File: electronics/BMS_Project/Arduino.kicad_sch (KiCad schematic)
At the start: 1 part

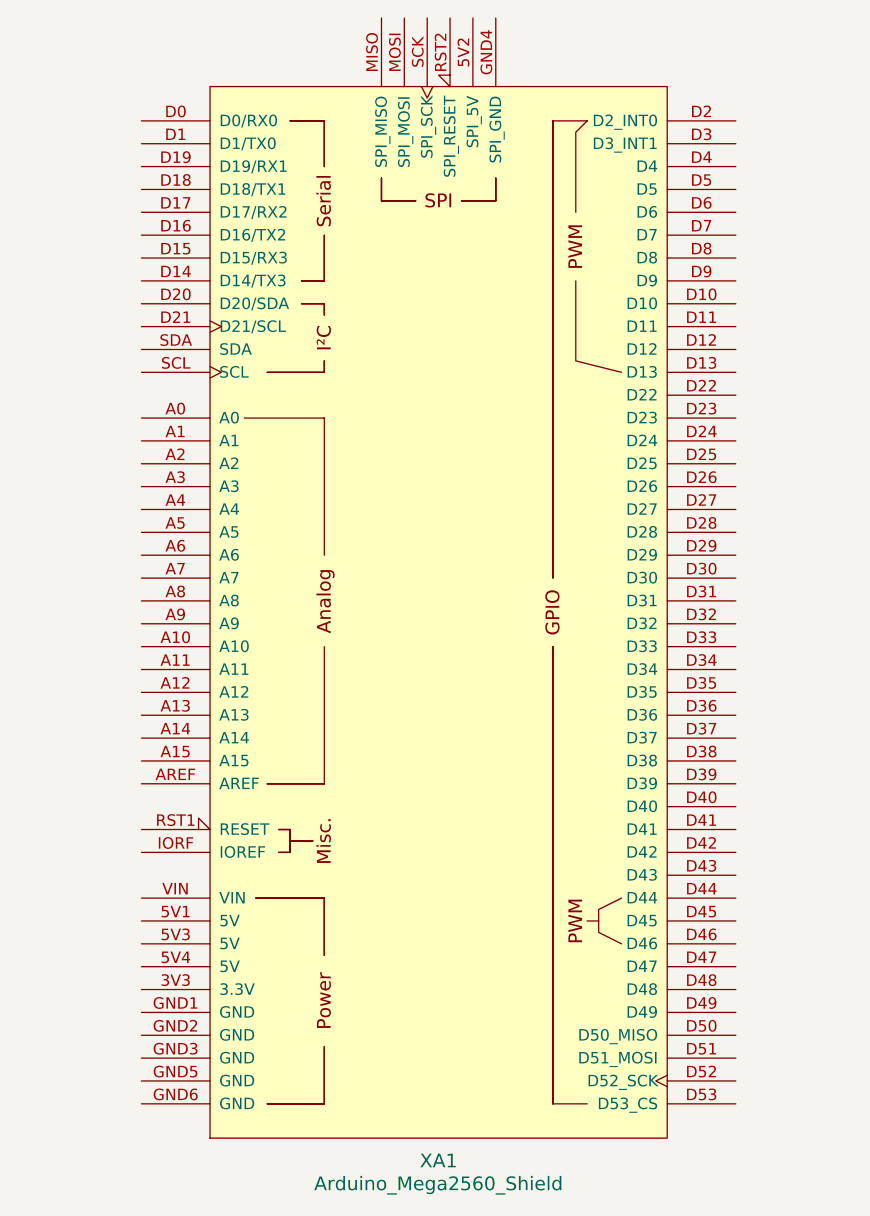
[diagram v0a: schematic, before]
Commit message: Started working on schematic segmentation and added first labels
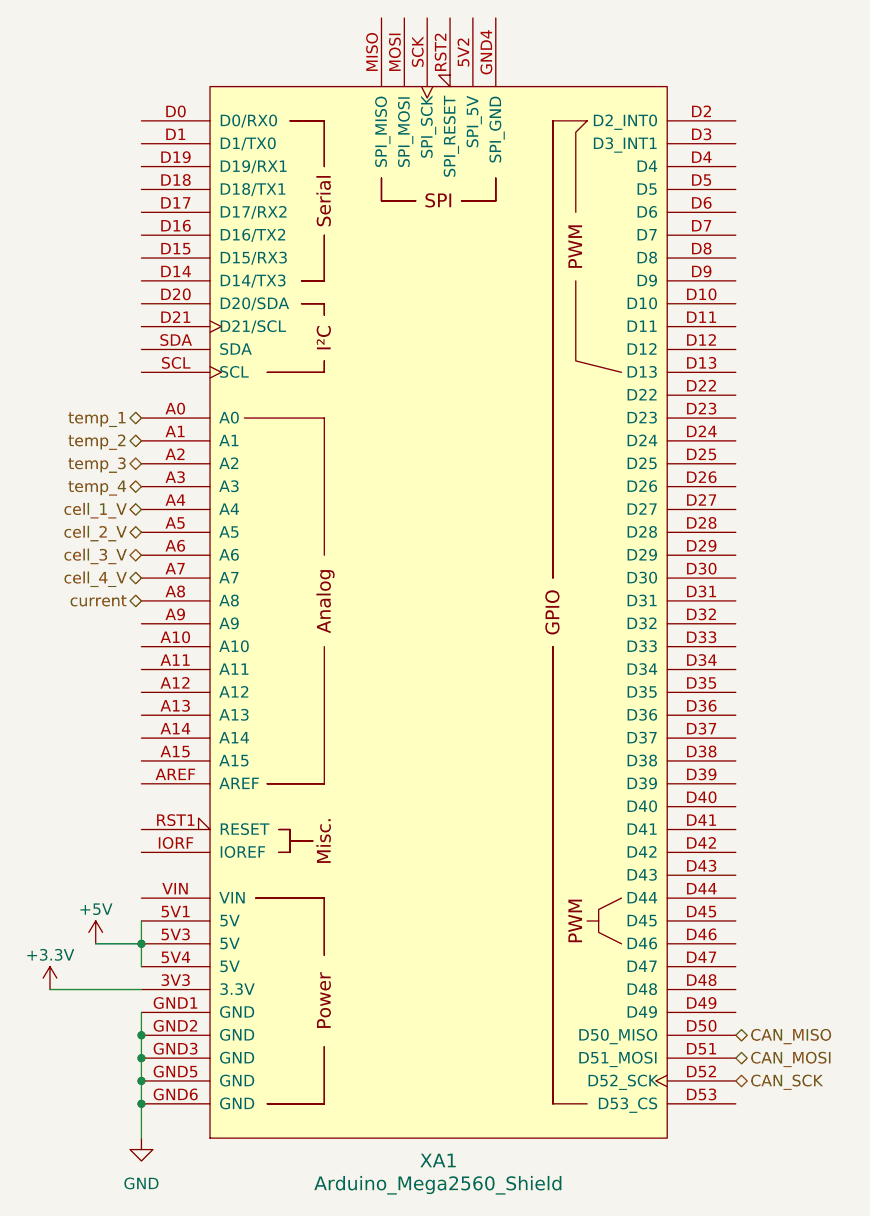
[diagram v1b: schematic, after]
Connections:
- net +3.3V: now reaches XA1.3V3 (3.3V)
- net +5V: now reaches XA1.5V1 (5V)
- net +5V: now also XA1.5V3 (5V), XA1.5V4 (5V)
- net temp_1: now reaches XA1.A0
- net temp_2: now reaches XA1.A1
- net temp_3: now reaches XA1.A2
- net temp_4: now reaches XA1.A3
- net cell_1_V: now reaches XA1.A4
- net cell_2_V: now reaches XA1.A5
- net cell_3_V: now reaches XA1.A6
- net cell_4_V: now reaches XA1.A7
- net current: now reaches XA1.A8
- net CAN_MISO: now reaches XA1.D50 (D50_MISO)
- net CAN_MOSI: now reaches XA1.D51 (D51_MOSI)
- net CAN_SCK: now reaches XA1.D52 (D52_SCK)
- net GND: now reaches XA1.GND1 (GND)
- net GND: now also XA1.GND2 (GND), XA1.GND3 (GND), XA1.GND5 (GND), XA1.GND6 (GND)
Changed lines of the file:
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@@
     (comment 2 "Edited: ")
+  )
+  (junction (at 82.55 132.08) (diameter 0) (color 0 0 0 0)
+  )
+  (junction (at 82.55 149.86) (diameter 0) (color 0 0 0 0)
+  )
+  (junction (at 82.55 142.24) (diameter 0) (color 0 0 0 0)
+  )
+  (junction (at 82.55 147.32) (diameter 0) (color 0 0 0 0)
+  )
+  (junction (at 82.55 144.78) (diameter 0) (color 0 0 0 0)
+  )
+  (wire (pts (xy 82.55 139.7) (xy 82.55 142.24))
+    (stroke (width 0) (type default))
+  )
+  (wire (pts (xy 82.55 147.32) (xy 82.55 149.86))
+    (stroke (width 0) (type default))
+  )
+  (wire (pts (xy 72.39 137.16) (xy 82.55 137.16))
+    (stroke (width 0) (type default))
+  )
+  (wire (pts (xy 77.47 132.08) (xy 82.55 132.08))
+    (stroke (width 0) (type default))
+  )
+  (wire (pts (xy 82.55 142.24) (xy 82.55 144.78))
+    (stroke (width 0) (type default))
+  )
+  (wire (pts (xy 82.55 149.86) (xy 82.55 153.67))
+    (stroke (width 0) (type default))
+  )
+  (wire (pts (xy 82.55 132.08) (xy 82.55 134.62))
+    (stroke (width 0) (type default))
+  )
+  (wire (pts (xy 82.55 129.54) (xy 82.55 132.08))
+    (stroke (width 0) (type default))
+  )
+  (wire (pts (xy 82.55 144.78) (xy 82.55 147.32))
+    (stroke (width 0) (type default))
+  )
+  (hierarchical_label "temp_1" (shape bidirectional) (at 82.55 73.66 180) (fields_autoplaced)
+    (effects (font (size 1.27 1.27)) (justify right))
+  )
+  (hierarchical_label "CAN_MOSI" (shape bidirectional) (at 148.59 144.78 0) (fields_autoplaced)
+    (effects (font (size 1.27 1.27)) (justify left))
+  )
+  (hierarchical_label "current" (shape bidirectional) (at 82.55 93.98 180) (fields_autoplaced)
+    (effects (font (size 1.27 1.27)) (justify right))
+  )
+  (hierarchical_label "cell_1_V" (shape bidirectional) (at 82.55 83.82 180) (fields_autoplaced)
+    (effects (font (size 1.27 1.27)) (justify right))
+  )
+  (hierarchical_label "temp_3" (shape bidirectional) (at 82.55 78.74 180) (fields_autoplaced)
+    (effects (font (size 1.27 1.27)) (justify right))
+  )
+  (hierarchical_label "cell_3_V" (shape bidirectional) (at 82.55 88.9 180) (fields_autoplaced)
+    (effects (font (size 1.27 1.27)) (justify right))
+  )
+  (hierarchical_label "temp_4" (shape bidirectional) (at 82.55 81.28 180) (fields_autoplaced)
+    (effects (font (size 1.27 1.27)) (justify right))
+  )
+  (hierarchical_label "cell_2_V" (shape bidirectional) (at 82.55 86.36 180) (fields_autoplaced)
+    (effects (font (size 1.27 1.27)) (justify right))
+  )
+  (hierarchical_label "cell_4_V" (shape bidirectional) (at 82.55 91.44 180) (fields_autoplaced)
+    (effects (font (size 1.27 1.27)) (justify right))
+  )
+  (hierarchical_label "CAN_MISO" (shape bidirectional) (at 148.59 142.24 0) (fields_autoplaced)
+    (effects (font (size 1.27 1.27)) (justify left))
+  )
+  (hierarchical_label "temp_2" (shape bidirectional) (at 82.55 76.2 180) (fields_autoplaced)
+    (effects (font (size 1.27 1.27)) (justify right))
+  )
+  (hierarchical_label "CAN_SCK" (shape bidirectional) (at 148.59 147.32 0) (fields_autoplaced)
+    (effects (font (size 1.27 1.27)) (justify left))
+  )
+  (symbol (lib_id "power:+3.3V") (at 72.39 137.16 0) (unit 1)
+    (in_bom yes) (on_board yes) (dnp no) (fields_autoplaced)
+    (property "Reference" "#PWR023" (at 72.39 140.97 0)
+      (effects (font (size 1.27 1.27)) hide)
+    )
+    (property "Value" "+3.3V" (at 72.39 133.35 0)
+      (effects (font (size 1.27 1.27)))
+    )
+    (property "Footprint" "" (at 72.39 137.16 0)
+      (effects (font (size 1.27 1.27)) hide)
+    )
+    (property "Datasheet" "" (at 72.39 137.16 0)
+      (effects (font (size 1.27 1.27)) hide)
+    )
+    (pin "1")
+    (instances
+      (project "BMS_Project"
+        (path "/524e7f14-feb0-4ca2-9425-a347c869bfa6/991268b7-e362-463f-9f04-bcec0fe70615"
+          (reference "#PWR023") (unit 1)
+        )
+      )
+    )
+  )
+  (symbol (lib_id "power:GND") (at 82.55 153.67 0) (unit 1)
+    (in_bom yes) (on_board yes) (dnp no) (fields_autoplaced)
+    (property "Reference" "#PWR022" (at 82.55 160.02 0)
+      (effects (font (size 1.27 1.27)) hide)
+    )
+    (property "Value" "GND" (at 82.55 158.75 0)
+      (effects (font (size 1.27 1.27)))
+    )
+    (property "Footprint" "" (at 82.55 153.67 0)
+      (effects (font (size 1.27 1.27)) hide)
+    )
+    (property "Datasheet" "" (at 82.55 153.67 0)
+      (effects (font (size 1.27 1.27)) hide)
+    )
+    (pin "1")
+    (instances
+      (project "BMS_Project"
+        (path "/524e7f14-feb0-4ca2-9425-a347c869bfa6/991268b7-e362-463f-9f04-bcec0fe70615"
+          (reference "#PWR022") (unit 1)
+        )
+      )
+    )
+  )
+  (symbol (lib_id "power:+5V") (at 77.47 132.08 0) (unit 1)
+    (in_bom yes) (on_board yes) (dnp no) (fields_autoplaced)
+    (property "Reference" "#PWR024" (at 77.47 135.89 0)
+      (effects (font (size 1.27 1.27)) hide)
+    )
+    (property "Value" "+5V" (at 77.47 128.27 0)
+      (effects (font (size 1.27 1.27)))
+    )
+    (property "Footprint" "" (at 77.47 132.08 0)
+      (effects (font (size 1.27 1.27)) hide)
+    )
+    (property "Datasheet" "" (at 77.47 132.08 0)
+      (effects (font (size 1.27 1.27)) hide)
+    )
+    (pin "1")
+    (instances
+      (project "BMS_Project"
+        (path "/524e7f14-feb0-4ca2-9425-a347c869bfa6/991268b7-e362-463f-9f04-bcec0fe70615"
+          (reference "#PWR024") (unit 1)
+        )
+      )
+    )
   )
   (symbol (lib_id "arduino-library:Arduino_Mega2560_Shield") (at 115.57 95.25 0) (unit 1)
